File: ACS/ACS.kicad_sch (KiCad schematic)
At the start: 13 parts, among them J1 Screw_Terminal_01x02, Q1 IRLB8721PBF, Q2 IRLB8721PBF, SW1 SW_SPDT, U1 Teensy4.1

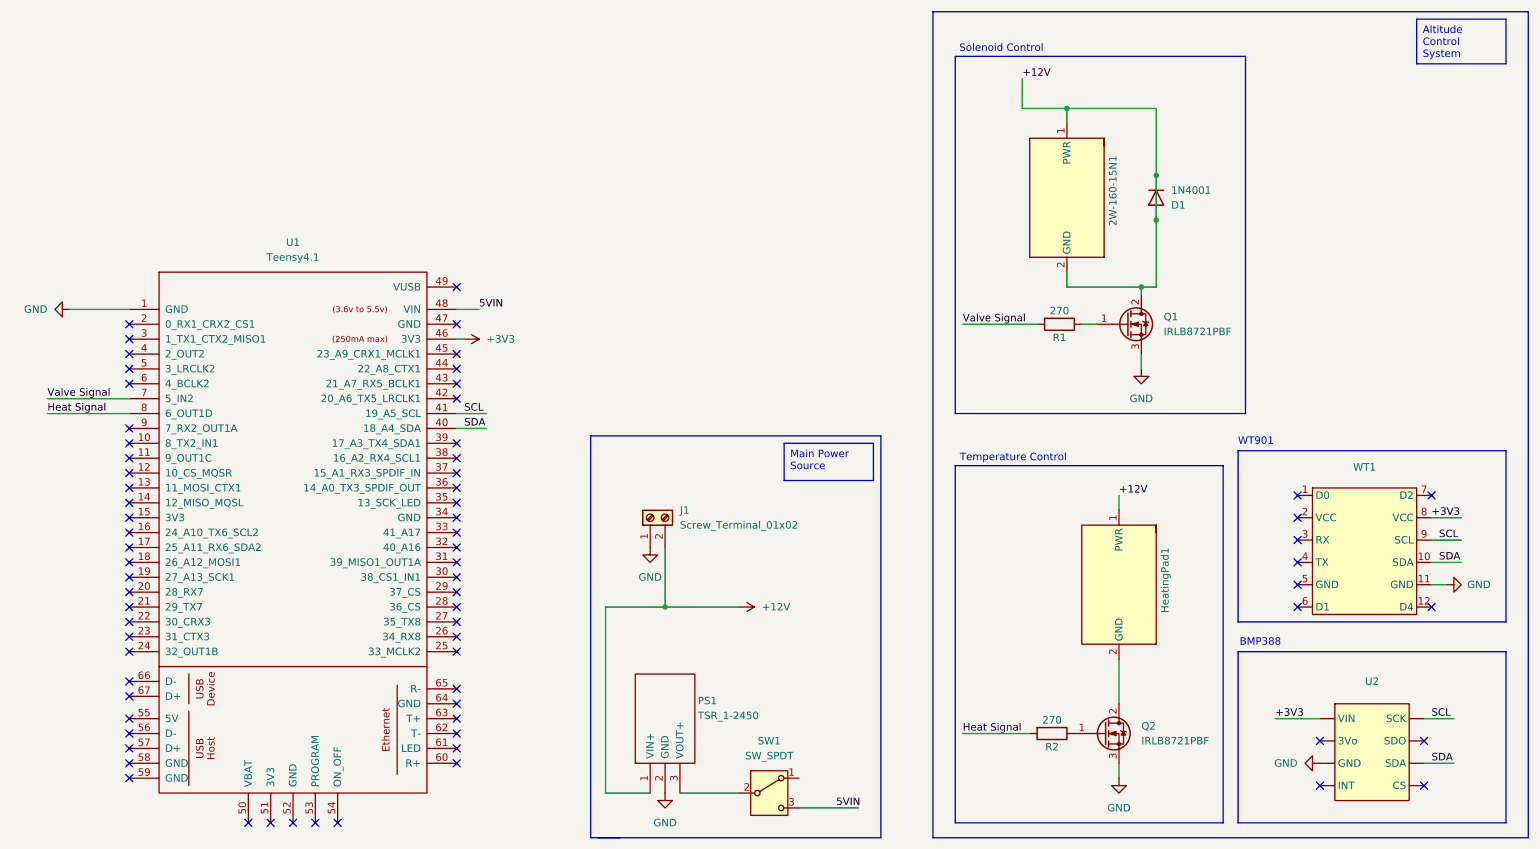
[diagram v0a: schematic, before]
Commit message: fixed error for U2
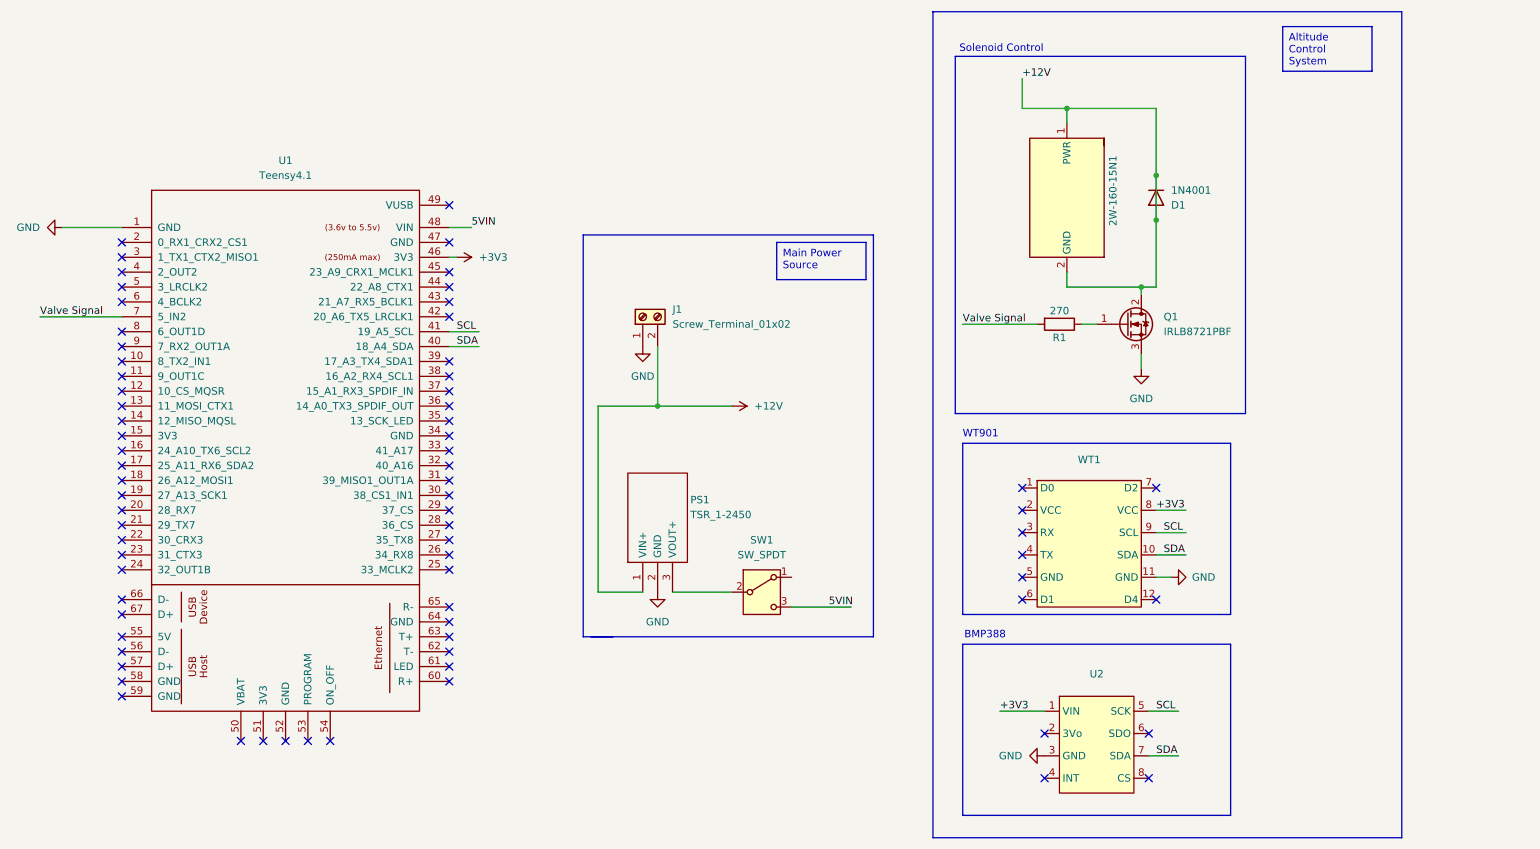
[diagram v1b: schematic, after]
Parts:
- removed HeatingPad1: ~, TerminalBlock_RND:TerminalBlock_RND_205-00276_1x02_P5.00mm_Vertical, symbol GRS_Valve:2W-160-15
- removed Q2: IRLB8721PBF, Package_TO_SOT_THT:TO-220-3_Vertical, symbol Transistor_FET:IRLB8721PBF
- removed R2: 270, Capacitor_THT:CP_Axial_L10.0mm_D4.5mm_P15.00mm_Horizontal, symbol Device:R
- SW1: footprint (none) -> TerminalBlock_RND:TerminalBlock_RND_205-00276_1x02_P5.00mm_Vertical
- WT1: footprint (none) -> Library:WT901
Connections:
- net +3V3: now also U2.1 (VIN); no longer U2. (VIN)
- net GND: now also U2.3 (GND); no longer U2. (VIN)
- net SCL: now also U2.5 (SCK); no longer U2. (VIN)
- net SDA: now also U2.7 (SDA); no longer U2. (VIN)
- net Heat Signal: no longer names the net of U1.8 (6_OUT1D)
- no-connect marks 72 -> 73
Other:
- note removed: "Temperature Control"
- moved on the sheet: J1, PS1, SW1, U1, WT1

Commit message: Updated screw terminal and switch design
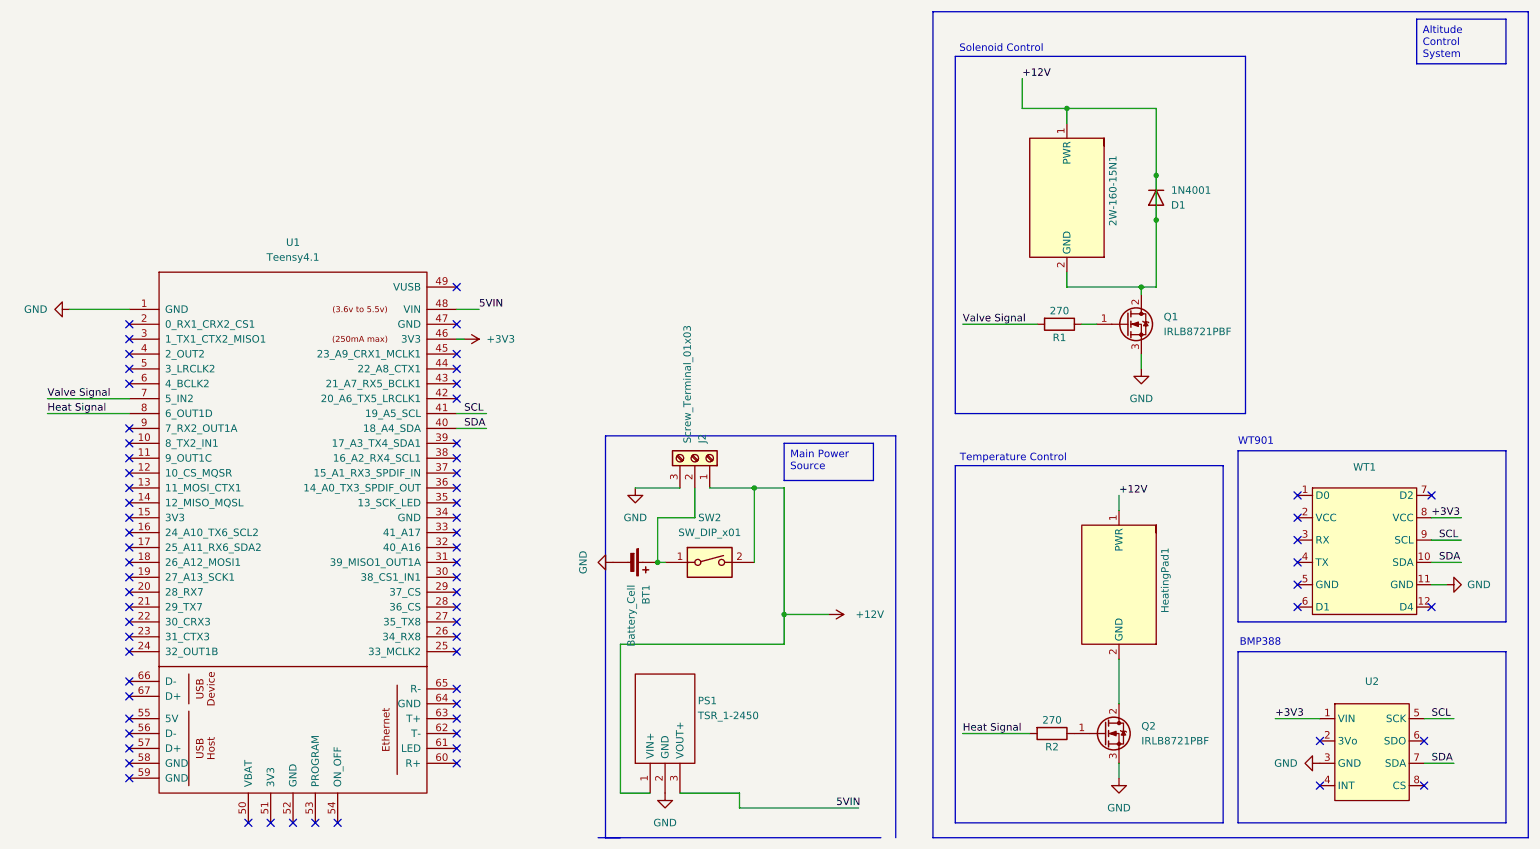
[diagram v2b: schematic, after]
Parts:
- removed J1: Screw_Terminal_01x02, TerminalBlock_RND:TerminalBlock_RND_205-00276_1x02_P5.00mm_Vertical, symbol Connector:Screw_Terminal_01x02
- removed SW1: SW_SPDT, TerminalBlock_RND:TerminalBlock_RND_205-00276_1x02_P5.00mm_Vertical, symbol Switch:SW_SPDT
- added BT1: Battery_Cell, symbol Device:Battery_Cell
- added HeatingPad1: ~, TerminalBlock_RND:TerminalBlock_RND_205-00276_1x02_P5.00mm_Vertical, symbol GRS_Valve:2W-160-15
- added J2: Screw_Terminal_01x03, symbol Connector:Screw_Terminal_01x03
- added Q2: IRLB8721PBF, Package_TO_SOT_THT:TO-220-3_Vertical, symbol Transistor_FET:IRLB8721PBF
- added R2: 270, Capacitor_THT:CP_Axial_L10.0mm_D4.5mm_P15.00mm_Horizontal, symbol Device:R
- added SW2: SW_DIP_x01, symbol Switch:SW_DIP_x01
- WT1: footprint Library:WT901 -> (none)
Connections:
- net +12V: now also HeatingPad1.1 (PWR), J2.1 (Pin_1), SW2.2
- net 5VIN: now also PS1.3 (VOUT+)
- net GND: now also BT1.2 (-), J2.3 (Pin_3), Q2.3 (S)
- net Heat Signal: now reaches U1.8 (6_OUT1D)
- net Heat Signal: now also R2.2
- new net: HeatingPad1.2 (GND), Q2.2 (D)
- new net: Q2.1 (G), R2.1
- new net: BT1.1 (+), J2.2 (Pin_2), SW2.1
- no-connect marks 73 -> 72
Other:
- note added: "Temperature Control"
- moved on the sheet: PS1, U1, U2, WT1
